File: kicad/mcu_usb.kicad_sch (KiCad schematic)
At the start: 46 parts, among them J4 USB-A host, SW2 BOOT, SW3 RESET, U10 RP2354A, U11 USBLC6-2SC6, U12 TPS2051C, U6 USBLC6-2SC6, Y1 12MHz

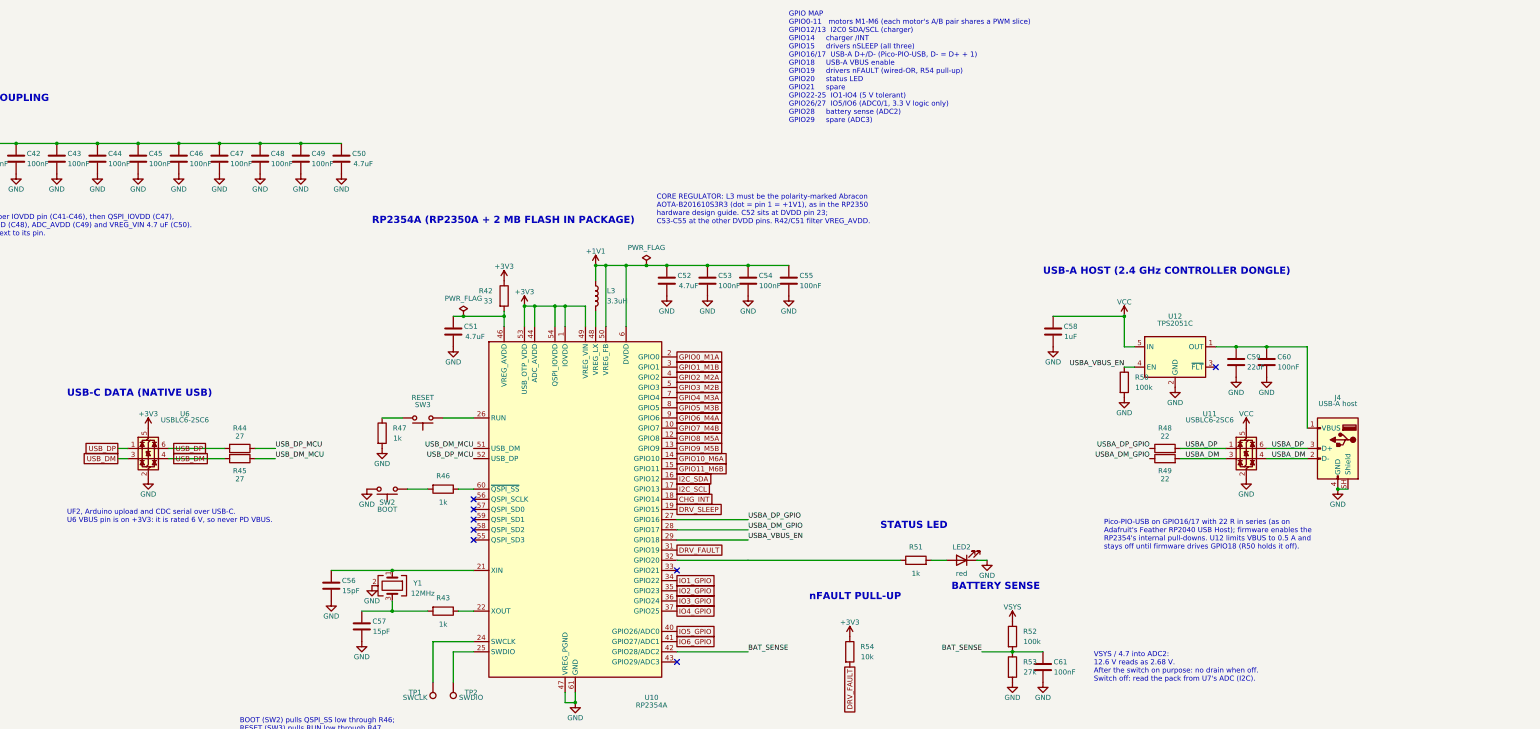
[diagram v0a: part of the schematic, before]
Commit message: Lay out rev 2 with an internal pack, protector and cost-down parts
Board is 91 x 47 mm for a 96 x 52 mm enclosure, with placement and hand
power routing done; signal routing is still to do.

- Internal Gens Ace 3S 1000 mAh pack on an XT60 pigtail, protected on the
  board by a BQ7791501 with back-to-back low-side FETs and a 2.5 mOhm
  shunt, plus a balance header and two NTCs.
- USB-A and USB-C on the top edge, IO as a recessed 3 x 6 pin block, GPIO
  map re-swapped for the placement, USB nets renamed with P/N suffixes
  for the diff-pair router.
- Cost-down swaps that keep every feature: basic or preferred passives
  and ICs, cheaper connectors, a THT power switch rated for 12.6 V, and
  replacements for the low-stock TH1 and Q2/Q3. L3 is Digi-Key sourced
  and hand-placed.
- Net classes and design rules, rev 2 power-net widths in review.py, and
  the PCB critic and loop updated for rev 2.

Schematic review passes; PCB review passes every gate except unrouted.

Co-Authored-By: Claude Opus 5.5 <noreply@anthropic.com>
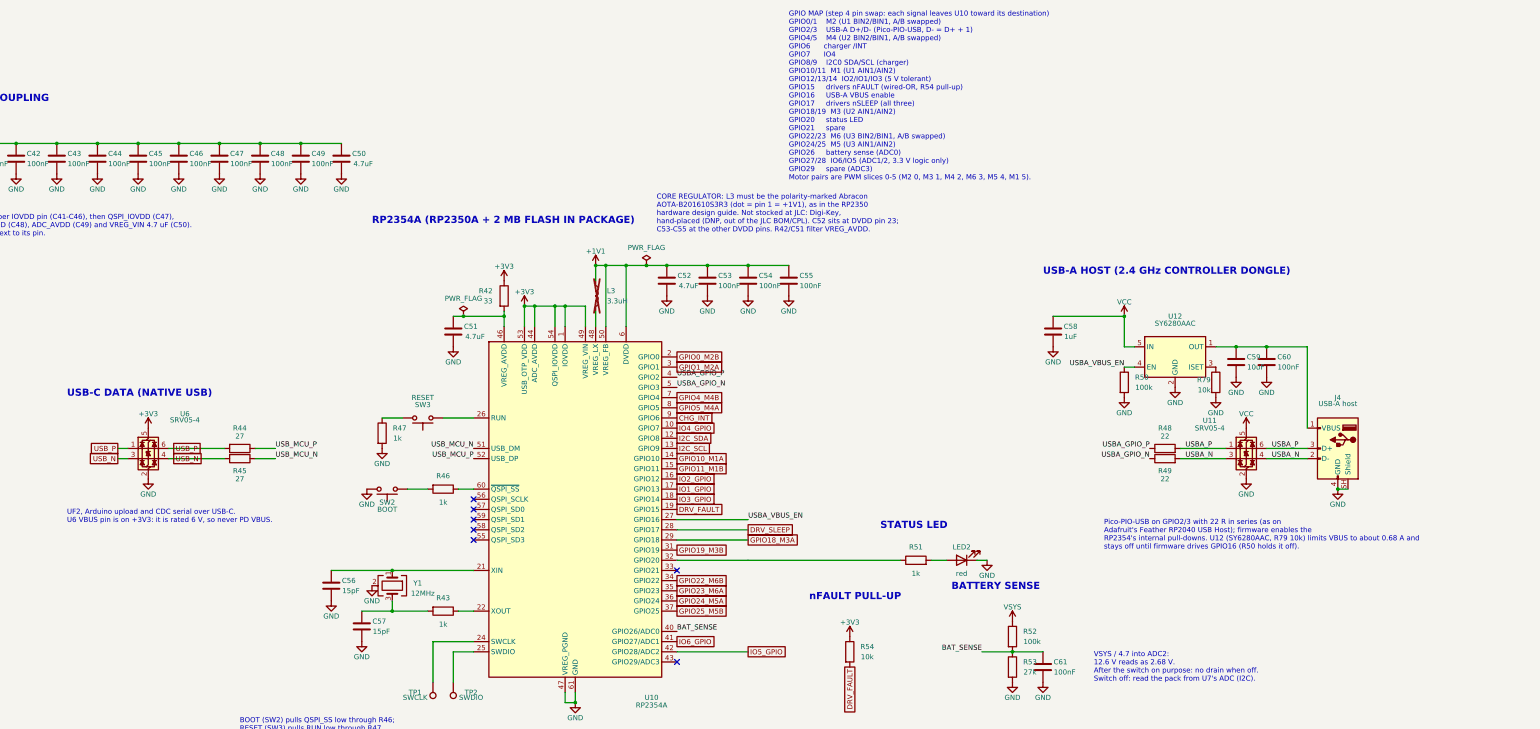
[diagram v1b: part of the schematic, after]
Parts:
- added R79: 10k, Resistor_SMD:R_0402_1005Metric, symbol Device:R
- C59: value 22uF -> 10uF; LCSC Part # C45783 -> C15850; MPN CL21A226MAQNNNE -> CL21A106KAYNNNE
- J4: footprint hexy:USB_A_Amphenol_87520-0010BLF -> hexy:USB_A_ShouHan_AF90_WJDG; LCSC Part # C599115 -> C456018; MPN 87520-0010BLF -> AF 90 WJDG; Manufacturer Amphenol ICC -> SHOU HAN
- L3: now not fitted; now left out of the parts list
- R44, R45: footprint Resistor_SMD:R_0402_1005Metric -> Resistor_SMD:R_0603_1608Metric; LCSC Part # C25100 -> C25190; MPN 0402WGF270JTCE -> 0603WAF270JT5E
- U11, U6: value USBLC6-2SC6 -> SRV05-4; symbol Power_Protection:USBLC6-2SC6 -> hexyhustle:SRV05-4; LCSC Part # C7519 -> C7420376; MPN USBLC6-2SC6 -> SRV05-4; Manufacturer STMicroelectronics -> hongjiacheng
- U12: value TPS2051C -> SY6280AAC; symbol Power_Management:TPS2051CDBV -> hexyhustle:SY6280AAC; LCSC Part # C129581 -> C55136; MPN TPS2051CDBVR -> SY6280AAC; Manufacturer Texas Instruments -> Silergy Corp
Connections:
- net GPIO6_M4A is gone; now on net CHG_INT: U10.9 (GPIO6)
- net GPIO7_M4B is gone; now on net IO4_GPIO: U10.10 (GPIO7)
- net GPIO8_M5A is gone; now on net I2C_SDA: U10.12 (GPIO8)
- net GPIO9_M5B is gone; now on net I2C_SCL: U10.13 (GPIO9)
- net BAT_SENSE: now also U10.40 (GPIO26/ADC0); no longer U10.42 (GPIO28/ADC2)
- net CHG_INT: no longer U10.18 (GPIO14)
- net DRV_FAULT: now also U10.19 (GPIO15); no longer U10.31 (GPIO19)
- net DRV_SLEEP: now also U10.28 (GPIO17); no longer U10.19 (GPIO15)
- net GND: now also R79.2
- net I2C_SCL: no longer U10.17 (GPIO13)
- net I2C_SDA: no longer U10.16 (GPIO12)
- net IO1_GPIO: now also U10.17 (GPIO13); no longer U10.34 (GPIO22)
- net IO2_GPIO: now also U10.16 (GPIO12); no longer U10.35 (GPIO23)
- net IO3_GPIO: now also U10.18 (GPIO14); no longer U10.36 (GPIO24)
- net IO4_GPIO: no longer U10.37 (GPIO25)
- net IO5_GPIO: now also U10.42 (GPIO28/ADC2); no longer U10.40 (GPIO26/ADC0)
- net USBA_VBUS_EN: now also U10.27 (GPIO16); no longer U10.29 (GPIO18)
- net at U12.3 (ISET): now also R79.1
- net GPIO0_M1A renamed GPIO0_M2B
- net GPIO10_M6A renamed GPIO10_M1A
- net GPIO11_M6B renamed GPIO11_M1B
- net GPIO1_M1B renamed GPIO1_M2A
- net GPIO2_M2A renamed USBA_GPIO_P
- net USBA_GPIO_P: now also R48.1
- net GPIO3_M2B renamed USBA_GPIO_N
- net USBA_GPIO_N: now also R49.1
- net GPIO4_M3A renamed GPIO4_M4B
- net GPIO5_M3B renamed GPIO5_M4A
- net USBA_DM renamed USBA_N
- removed net USBA_DM_GPIO: R49.1, U10.28 (GPIO17)
- net USBA_DP renamed USBA_P
- removed net USBA_DP_GPIO: R48.1, U10.27 (GPIO16)
- net USB_DM renamed USB_N
- net USB_DM_MCU renamed USB_MCU_N
- net USB_DP renamed USB_P
- net USB_DP_MCU renamed USB_MCU_P
- new net GPIO18_M3A: U10.29 (GPIO18)
- new net GPIO19_M3B: U10.31 (GPIO19)
- new net GPIO22_M6B: U10.34 (GPIO22)
- new net GPIO23_M6A: U10.35 (GPIO23)
- new net GPIO24_M5A: U10.36 (GPIO24)
- new net GPIO25_M5B: U10.37 (GPIO25)
- no-connect marks 8 -> 7
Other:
- note added: "CORE REGULATOR: L3 must be the polarity-marked Abracon AOTA-B201610S3R3 (dot = pin 1 = +1V1), as in the RP2350 hardware design guide. Not stocked at JLC: Digi-Key, hand-placed (DNP, out of the JLC BOM/CPL). C52 sits at DVDD pin 23; C53-C55 at the other DVDD pins. R42/C51 filter VREG_AVDD."
- note added: "GPIO MAP (step 4 pin swap: each signal leaves U10 toward its destination) GPIO0/1 M2 (U1 BIN2/BIN1, A/B swapped) GPIO2/3 USB-A D+/D- (Pico-PIO-USB, D- = D+ + 1) GPIO4/5 M4 (U2 BIN2/BIN1, A/B swapped) GPIO6 charger /INT GPIO7 IO4 GPIO8/9 I2C0 SDA/SCL (charger) GPIO10/11 M1 (U1 AIN1/AIN2) GPIO12/13/14 IO2/IO1/IO3 (5 V tolerant) GPIO15 drivers nFAULT (wired-OR, R54 pull-up) GPIO16 USB-A VBUS enable 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"
- note added: "Pico-PIO-USB on GPIO2/3 with 22 R in series (as on Adafruit's Feather RP2040 USB Host); firmware enables the RP2354's internal pull-downs. U12 (SY6280AAC, R79 10k) limits VBUS to about 0.68 A and stays off until firmware drives GPIO16 (R50 holds it off)."
- note removed: "CORE REGULATOR: L3 must be the polarity-marked Abracon AOTA-B201610S3R3 (dot = pin 1 = +1V1), as in the RP2350 hardware design guide. C52 sits at DVDD pin 23; C53-C55 at the other DVDD pins. R42/C51 filter VREG_AVDD."
- note removed: "GPIO MAP GPIO0-11 motors M1-M6 (each motor's A/B pair shares a PWM slice) GPIO12/13 I2C0 SDA/SCL (charger) GPIO14 charger /INT GPIO15 drivers nSLEEP (all three) GPIO16/17 USB-A D+/D- (Pico-PIO-USB, D- = D+ + 1) GPIO18 USB-A VBUS enable GPIO19 drivers nFAULT (wired-OR, R54 pull-up) GPIO20 status LED GPIO21 spare GPIO22-25 IO1-IO4 (5 V tolerant) GPIO26/27 IO5/IO6 (ADC0/1, 3.3 V logic only) GPIO28 b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"
- note removed: "Pico-PIO-USB on GPIO16/17 with 22 R in series (as on Adafruit's Feather RP2040 USB Host); firmware enables the RP2354's internal pull-downs. U12 limits VBUS to 0.5 A and stays off until firmware drives GPIO18 (R50 holds it off)."

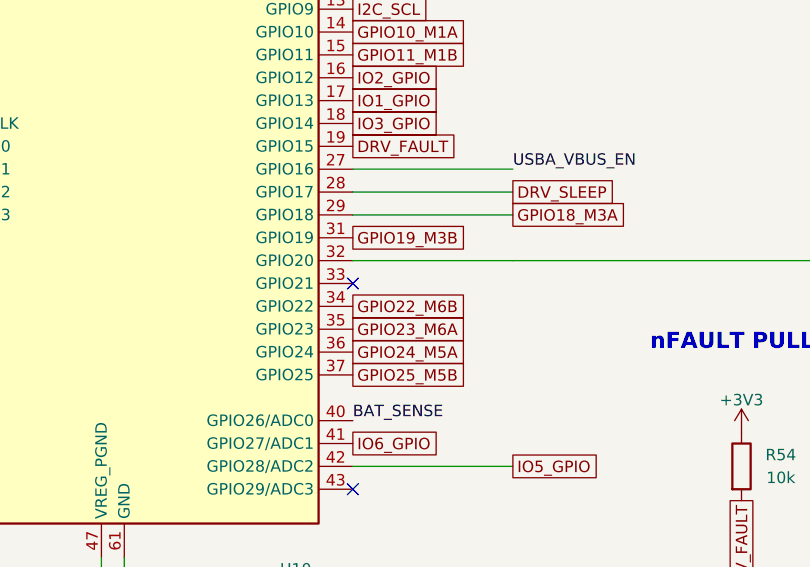
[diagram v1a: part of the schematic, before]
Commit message: Add a header for an external WS2812B LED stick
J12 (JST-PH 3-pin) feeds an 8-LED WS2812B stick mounted on the case's
top edge near the USB ports. GPIO21 drives it through a 74AHCT1G125 so
the data line reaches the 5 V VIH, with a 330 ohm series resistor and
10 uF at the connector. Power comes from the switched 5 V rail; firmware
should cap brightness (about 0.5 A at full white).

Co-Authored-By: Claude Opus 5.5 <noreply@anthropic.com>
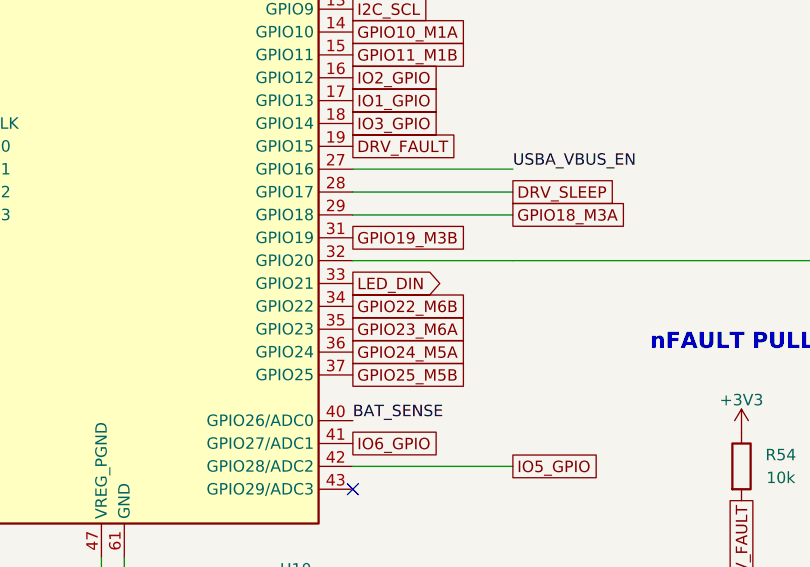
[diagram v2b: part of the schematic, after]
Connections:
- net LED_DIN: now reaches U10.33 (GPIO21)
- no-connect marks 7 -> 6
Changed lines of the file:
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@@
 	)
 	(no_connect
-		(at 215.9 170.18)
-	)
-	(no_connect
 		(at 215.9 193.04)
 	)
@@
 		)
 	)
+	(global_label "LED_DIN"
+		(shape output)
+		(at 215.9 170.18 0)
+		(effects
+			(font
+				(size 1.27 1.27)
+			)
+			(justify left)
+		)
+	)
